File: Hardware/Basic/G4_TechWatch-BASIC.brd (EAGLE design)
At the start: 38 x 38 mm, 44 parts, among them U2 NRF52832_MODULE_MDBT42

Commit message: End Of Class Schematic
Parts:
- added C2: 1u, LinnesLab-Passives:C0603
- added R8, R9: 10k, LinnesLab-Passives:R0603
- added SW1, SW2, SW5: SWITCH.MOM, LinnesLab-Switches:TACTILE_SWITCH_SMD_6.2MM_TALL
- added U4: PCF8523, LinnesLab-Clocks:SO8
- added XTAL3: 32.7680kHz, LinnesLab-Clocks:2-SMD.NOLEAD.2.0MMTO1.2MM
- moved D5 10.8 mm to (12.0, 16.7)
- moved C20 10.8 mm to (17.6, 24.8)
- moved C21 10.8 mm to (23.6, 24.7)
- moved C5 10.8 mm to (16.9, 17.8)
- moved C6 10.8 mm to (23.0, 17.8)
- moved CHRG2 10.8 mm to (20.4, 24.8)
- moved D4 10.8 mm to (12.0, 18.8)
- moved LDO2 10.8 mm to (19.9, 17.7)
- moved R11 10.8 mm to (22.6, 27.4)
- moved R12 10.8 mm to (20.5, 21.8)
- moved R13 10.8 mm to (13.0, 27.6)
- moved R14 10.8 mm to (13.0, 24.3)
- moved C7 10.7 mm to (18.9, 35.3)
- moved C12 10.7 mm to (17.8, 31.3)
- moved L2 10.7 mm to (16.9, 35.5)
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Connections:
- new net N$16: SW1.A1, SW1.A2
- new net N$18: SW1.B1, SW1.B2
- new net N$19: U4.2, XTAL3.P$1
- new net N$20: U4.1, XTAL3.P$2
- new net N$22: SW2.A1, SW2.A2
- new net N$23: SW2.B1, SW2.B2
- new net N$24: SW5.A1, SW5.A2
- new net N$25: SW5.B1, SW5.B2
- new net VBATT: U4.3
- net 3.3V: now also C2.1, R8.2, R9.2, U4.8
- net GND: now also C2.2, U4.4
- net SCL: now also R8.1, U4.6
- net SDA: now also R9.1, U4.5

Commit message: Updated Schematics
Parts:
- moved SW5 44.6 mm to (31.0, 5.00), turned to 180 degrees
- moved SW2 30.2 mm to (19.0, 5.00), turned to 180 degrees
- moved C6 17.2 mm to (23.2, 35.0)
- moved R4 17.2 mm to (29.0, 13.8)
- moved SW1 15.8 mm to (7.00, 5.00), turned to 180 degrees
- moved R15 9.75 mm to (15.0, 13.9)
- moved C18 7.39 mm to (22.3, 30.5)
- moved C16 7.08 mm to (24.0, 30.5)
- moved R7 5.47 mm to (7.09, 14.1)
- moved R6 5.20 mm to (7.42, 16.9)
- moved R9 1.42 mm to (12.7, 33.1)
- moved XTAL3 0.89 mm to (2.51, 34.2)
- moved C2 0.53 mm to (8.51, 36.4)
- moved U4 0.47 mm to (6.71, 32.9)
- moved R8 0.25 mm to (11.2, 33.1)
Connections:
- net N$16 renamed SW1
- net N$22 renamed SW2
- net N$24 renamed SW3
- net VBATT renamed VBAT
- removed net N$18: SW1.B1, SW1.B2
- removed net N$23: SW2.B1, SW2.B2
- removed net N$25: SW5.B1, SW5.B2
- net GND: now also SW1.B1, SW1.B2, SW2.B1, SW2.B2, SW5.B1, SW5.B2, USB2.S1, USB2.S2, USB2.S3, USB2.S4, USB2.S5, USB2.S6
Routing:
- added copper zone on layer 16, net 3.3V
- added copper zone on layer 1, net GND

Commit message: Schematic Step 1 Done
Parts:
- removed SD2: (no value), LinnesLab-Connectors:MICROSD
- removed USB2: USB.MICRO-BIGGERPADS, LinnesLab-Connectors:USB-MICRO-01.BIGGERPADS
- added J1: FTDI_DEVICESMD, LinnesLab-Connectors:FTDI-SMD
- moved D1 22.2 mm to (25.2, 16.1)
- moved C14 22.0 mm to (27.9, 16.3)
- moved SW3 13.1 mm to (35.8, 34.9), turned to 270 degrees
- moved R13 11.9 mm to (1.32, 25.4)
- moved LED4 10.4 mm to (35.4, 20.2)
- moved R14 9.80 mm to (3.28, 25.2)
- moved R5 9.57 mm to (35.4, 17.1)
- moved SW4 9.05 mm to (32.2, 17.3)
- moved LED3 7.75 mm to (35.5, 22.3)
- moved CORTEX1 5.79 mm to (35.6, 29.1), turned to 270 degrees
- moved C15 5.32 mm to (2.74, 29.0)
- moved C17 5.32 mm to (5.41, 28.9)
- moved C13 5.32 mm to (1.35, 28.8)
- moved C19 5.32 mm to (4.09, 28.9)
- moved D4 3.94 mm to (11.9, 14.9)
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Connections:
- removed net CD1: SD2.CD1
- removed net CD2: SD2.CD2
- removed net SD.CS: SD2.2
- removed net USB+: USB2.3
- removed net USB-: USB2.2
- net 3.3V: no longer SD2.4
- net GND: no longer SD2.6, SD2.MT1, SD2.MT2, USB2.5, USB2.S1, USB2.S2, USB2.S3, USB2.S4, USB2.S5, USB2.S6
- net MISO: no longer SD2.7
- net MOSI: no longer SD2.3
- net SCK: no longer SD2.5
- net V_USB: no longer USB2.1

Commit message: End of Class 09/21/2022
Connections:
- removed net BATT: R13.1, R14.2
- new net AIN4/BATT: R13.1, R14.2, U2.5
- net CHRG.STAT: now also U2.4
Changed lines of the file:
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@@
 <drawing>
 <settings>
-<setting alwaysvectorfont="yes"/>
+<setting alwaysvectorfont="no"/>
 <setting verticaltext="up"/>
 </settings>
@@
 <contactref element="R12" pad="1"/>
 <contactref element="CHRG2" pad="1"/>
+<contactref element="U2" pad="4"/>
+<wire x1="17.1657" y1="25.715" x2="23.9496" y2="29.0164" width="0" layer="19" extent="1-1"/>
 <wire x1="17.6412" y1="21.844" x2="17.1657" y2="25.715" width="0" layer="19" extent="1-1"/>
-</signal>
-<signal name="BATT">
-<contactref element="R13" pad="1"/>
-<contactref element="R14" pad="2"/>
-<wire x1="1.3208" y1="24.5246" x2="3.2766" y2="26.0976" width="0" layer="19" extent="1-1"/>
 </signal>
 <signal name="VIN">
@@
 <contactref element="U4" pad="3"/>
 </signal>
+<signal name="AIN4/BATT">
+<contactref element="U2" pad="5"/>
+<contactref element="R13" pad="1"/>
+<contactref element="R14" pad="2"/>
+<wire x1="3.2766" y1="26.0976" x2="23.9496" y2="28.3164" width="0" layer="19" extent="1-1"/>
+<wire x1="1.3208" y1="24.5246" x2="3.2766" y2="26.0976" width="0" layer="19" extent="1-1"/>
+</signal>
 </signals>

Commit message: Weekly commit for class
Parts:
- moved R7 19.2 mm to (26.1, 16.5), turned to 270 degrees
- moved C18 18.6 mm to (27.1, 13.2)
- moved C6 18.0 mm to (7.14, 23.8)
- moved C17 15.5 mm to (14.1, 16.1), turned to 90 degrees
- moved C16 15.2 mm to (27.9, 16.5), turned to 90 degrees
- moved C15 14.9 mm to (10.9, 16.6)
- moved C19 14.8 mm to (12.3, 16.6), turned to 90 degrees
- moved C13 14.8 mm to (9.55, 16.6)
- moved XTAL2 11.7 mm to (25.4, 23.5), flipped to the bottom
- moved L2 10.4 mm to (19.5, 26.2), turned to 0 degrees
- moved R11 9.37 mm to (11.3, 28.9)
- moved R6 8.46 mm to (15.8, 16.3), turned to 90 degrees
- moved C7 8.20 mm to (19.5, 27.5), turned to 180 degrees
- moved C12 7.94 mm to (19.0, 24.1)
- moved C21 7.25 mm to (15.9, 29.2)
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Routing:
- net 3.3V: track 0.00 -> 19.1 mm, vias 0 -> 4
- net N$11: track 0.00 -> 5.85 mm
- net N$15: track 0.00 -> 5.50 mm
- net N$12: track 0.00 -> 5.15 mm
- net SDA: track 0.00 -> 3.88 mm
- net N$8: track 0.00 -> 3.68 mm
- net N$5: track 0.00 -> 3.68 mm
- net RESET: track 0.00 -> 2.40 mm
- net N$1: track 0.00 -> 2.17 mm
- net SWO: track 0.00 -> 2.16 mm
- net N$7: track 0.00 -> 2.09 mm
- net N$3: track 0.00 -> 2.09 mm
- net N$2: track 0.00 -> 2.04 mm
- net N$13: track 0.00 -> 1.99 mm
- net SCL: track 0.00 -> 1.83 mm
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
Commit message: Commit before leaving class
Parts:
- flipped XTAL2 to the top
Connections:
- removed net AIN4/BATT: R13.1, R14.2, U2.5
- new net AIN7/BATT: R13.1, R14.2, U2.8
- new net D7/SD.CS: U2.20
- net CS.OLED: now also U2.30
- net DC.OLED: now also U2.17
- net DTR: now also J1.DTR
- net GND: now also J1.CTS, J1.GND
- net RESET.OLED: now also U2.16
- net RXD: now also J1.TXO
- net SW1: now also U2.25
- net SW2: now also U2.29
- net SW3: now also U2.5
- net TXD: now also J1.RXI
- net V_USB: now also J1.VCC
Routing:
- net 3.3V: track 19.1 -> 0.00 mm, vias 4 -> 0
- net N$11: track 5.85 -> 0.00 mm
- net N$15: track 5.50 -> 0.00 mm
- net N$12: track 5.15 -> 0.00 mm
- net SDA: track 3.88 -> 0.00 mm
- net N$8: track 3.68 -> 0.00 mm
- net N$5: track 3.68 -> 0.00 mm
- net RESET: track 2.40 -> 0.00 mm
- net N$1: track 2.17 -> 0.00 mm
- net SWO: track 2.16 -> 0.00 mm
- net N$7: track 2.09 -> 0.00 mm
- net N$3: track 2.09 -> 0.00 mm
- net N$2: track 2.04 -> 0.00 mm
- net N$13: track 1.99 -> 0.00 mm
- net SCL: track 1.83 -> 0.00 mm
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
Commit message: Board Completed
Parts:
- removed C19: 2.2uF, LinnesLab-Passives:C0402
- removed C20, C21: 4.7u, LinnesLab-Passives:C0603
- removed CHRG2: MCP73831, LinnesLab-Power:SOT23-5
- removed CORTEX1: CORTEX_DEBUG_PTH, LinnesLab-Connectors:2X5-PTH-1.27MM
- removed D4, D5: (no value), LinnesLab-DiscreteSemi:USC
- removed L2: 10u, LinnesLab-Passives:L0603
- removed LDO2: MIC5504, LinnesLab-Power:SOT23-5
- removed LED3: RED, LinnesLab-LED:LED-0603
- removed LED4: BLUE, LinnesLab-LED:LED-0603
- removed R13, R14, R15: 100k, LinnesLab-Passives:R0603
- removed U4: PCF8523, LinnesLab-Clocks:SO8
- removed XTAL3: 32.7680kHz, LinnesLab-Clocks:2-SMD.NOLEAD.2.0MMTO1.2MM
- added C1: 1u, LinnesLab-Passives:C0603
- added C3, C4: (no value), LinnesLab-Passives:C0603
- added CHRG1: MCP73831, LinnesLab-Power:SOT23-5
- added D2, D3: (no value), LinnesLab-DiscreteSemi:USC
- added DEBUG1: CORTEX_DEBUG_PTH, LinnesLab-Connectors:2X5-PTH-1.27MM
- added L1: 10u, LinnesLab-Passives:L0603
- added LDO1: MIC5504, LinnesLab-Power:SOT23-5
- added LED1: RED, LinnesLab-LED:LED-0603
- added LED2: BLUE, LinnesLab-LED:LED-0603
- added R1, R10, R2: 10k, LinnesLab-Passives:R0603
- added U1: NRF52832_MODULE_MDBT42, LinnesLab-Microcontrollers:BLE_MODULE_RAYTAC_MDBT42
- added XTAL1: 32.768kHz, LinnesLab-Clocks:2-SMD.NOLEAD.2.0MMTO1.2MM
- C10: value 300p -> 4.7u
- C11: value 300p -> 100n
- C12: value 10u -> 10uF; device LinnesLab-Passives:C0805 -> LinnesLab-Passives:C0603
- C14: value 100n -> 2.2uF; device LinnesLab-Passives:C0603 -> LinnesLab-Passives:C0402
- C16: value 10uF -> 2.2uF; device LinnesLab-Passives:C0603 -> LinnesLab-Passives:C0402
- C18: value 2.2uF -> 1u; device LinnesLab-Passives:C0402 -> LinnesLab-Passives:C0603
- C2: value 1u -> 10u; device LinnesLab-Passives:C0603 -> LinnesLab-Passives:C0805
- C5, C6: value 1u -> 300p
- C7: value 1u -> 4.7u
- C8, C9: value (none) -> 1u
- R11: value (none) -> 10k
- R12: value 100k -> 390k
- R3: value 1k -> 100k
- R5: value 10k -> 1k
- R6: value 10k -> (none)
- R7: value 390k -> 100k
- R8, R9: value 10k -> 100k
- SW1, SW2: value SWITCH.MOM -> (none); device LinnesLab-Switches:TACTILE_SWITCH_SMD_6.2MM_TALL -> LinnesLab-Switches:BUTTON-GULLWING
- SW3, SW4: value (none) -> SWITCH.MOM; device LinnesLab-Switches:BUTTON-GULLWING -> LinnesLab-Switches:TACTILE_SWITCH_SMD_6.2MM_TALL
- U2: value NRF52832_MODULE_MDBT42 -> PCF8523; device LinnesLab-Microcontrollers:BLE_MODULE_RAYTAC_MDBT42 -> LinnesLab-Clocks:SO8
- XTAL2: value 32.768kHz -> 32.7680kHz
- moved SW1 41.6 mm to (35.0, 35.7), turned to 0 degrees
- moved SW3 37.7 mm to (12.7, 5.03), turned to 180 degrees
- moved R3 31.2 mm to (6.02, 14.5), turned to 270 degrees
- moved C10 30.7 mm to (4.62, 16.9), turned to 90 degrees
- moved C18 27.3 mm to (8.20, 32.9), turned to 180 degrees
- moved C9 26.5 mm to (3.89, 2.84), turned to 270 degrees
- moved R7 24.9 mm to (5.31, 2.84), turned to 90 degrees
- moved C6 24.9 mm to (31.7, 19.9), turned to 0 degrees
- moved XTAL2 24.3 mm to (2.21, 30.7), turned to 90 degrees
- moved R9 23.6 mm to (3.20, 11.2)
- moved U2 22.1 mm to (6.40, 29.4)
- moved C7 21.1 mm to (7.09, 10.4), turned to 90 degrees
- moved C8 20.9 mm to (4.67, 12.8), turned to 90 degrees
- moved R8 20.3 mm to (3.20, 14.2)
- moved SW2 19.7 mm to (34.9, 16.6), turned to 90 degrees
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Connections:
- net 3.3V: now also C16.2, C18.1, C2.2, C9.1, D3.-, DEBUG1.1, LDO1.5, R1.2, R10.2, R2.2, R7.2, U1.11, U2.8; no longer C12.2, C19.2, C2.1, C6.1, CORTEX1.1, D1.-, LDO2.5, R15.2, R5.2, R8.2, R9.2, U2.11, U4.8
- net AIN7/BATT: now also R8.1, R9.2, U1.8; no longer R13.1, R14.2, U2.8
- net CHRG.STAT: now also CHRG1.1, R3.1, U1.4; no longer CHRG2.1, R12.1, U2.4
- net CS.OLED: now also U1.30; no longer U2.30
- net D7/SD.CS: now also U1.20; no longer U2.20
- net DC.OLED: now also U1.17; no longer U2.17
- net DFU: now also SW1.3, U1.34; no longer SW3.3, U2.34
- net DTR: now also C11.1; no longer C14.1
- net FRST: now also U1.38; no longer U2.38
- net GND: now also C1.2, C14.1, C18.2, C2.1, C3.1, C4.2, C5.2, C7.1, CHRG1.2, DEBUG1.3, DEBUG1.5, DEBUG1.7, DEBUG1.9, LDO1.2, LED1.C, LED2.C, R12.2, R7.1, R9.1, SW1.1, SW2.3, SW3.B1, SW3.B2, SW4.B1, SW4.B2, U1.1, U1.12, U1.24, U1.39, U2.4; no longer C11.2, C18.1, C19.1, C2.2, C20.2, C21.1, C5.1, C7.2, CHRG2.2, CORTEX1.3, CORTEX1.5, CORTEX1.7, CORTEX1.9, LDO2.2, LED3.C, LED4.C, R14.1, R15.1, R7.2, SW1.B1, SW1.B2, SW2.B1, SW2.B2, SW3.1, SW4.3, U2.1, U2.12, U2.24, U2.39, U4.4
- net LED1: now also R4.2, U1.31; no longer R3.2, U2.31
- net LED2: now also R5.2, U1.33; no longer R4.2, U2.33
- net MISO: now also U1.28; no longer U2.28
- net MOSI: now also U1.27; no longer U2.27
- net N$1: now also R11.2; no longer R6.2
- net N$10: now also LED2.A, R5.1; no longer LED4.A, R4.1
- net N$11: now also L1.1, U1.10; no longer L2.1, U2.10
- net N$12: now also C1.1, L1.2, U1.9; no longer C7.1, L2.2, U2.9
- net N$13: now also C12.2; no longer C16.2
- net N$14: now also DEBUG1.8; no longer CORTEX1.8
- net N$15: now also C14.2; no longer C18.2
- net N$17: now also CHRG1.5, R6.2; no longer CHRG2.5, R11.2
- net N$19: now also U2.2, XTAL2.P$1; no longer U4.2, XTAL3.P$1
- net N$2: now also R12.1; no longer R7.1
- net N$20: now also U2.1, XTAL2.P$2; no longer U4.1, XTAL3.P$2
- net N$3: now also C15.2; no longer C13.2
- net N$4: now also C3.2, U1.13, XTAL1.P$1; no longer C8.2, U2.13, XTAL2.P$1
- net N$5: now also C15.1; no longer C13.1
- net N$6: now also C4.1, U1.14, XTAL1.P$2; no longer C9.1, U2.14, XTAL2.P$2
- net N$7: now also C13.2; no longer C15.2
- net N$8: now also C13.1; no longer C15.1
- net N$9: now also LED1.A, R4.1; no longer LED3.A, R3.1
- net P0.09/NFC1: now also C5.1, U1.22; no longer C11.1, U2.22
- net P0.10/NFC2: now also C6.1, U1.23; no longer C10.1, U2.23
- net RESET: now also C11.2, D3.+, DEBUG1.10, R10.1, SW2.1, U1.35; no longer C14.2, CORTEX1.10, D1.+, R5.1, SW4.1, U2.35
- net RESET.OLED: now also U1.16; no longer U2.16
- net RXD: now also U1.21; no longer U2.21
- net SCK: now also U1.26; no longer U2.26
- net SCL: now also R2.1, U1.3, U2.6; no longer R8.1, U2.3, U4.6
- net SDA: now also R1.1, U1.2, U2.5; no longer R9.1, U2.2, U4.5
- net SW1: now also SW3.A1, SW3.A2, U1.25; no longer SW1.A1, SW1.A2, U2.25
- net SW2: now also SW4.A1, SW4.A2, U1.29; no longer SW2.A1, SW2.A2, U2.29
- net SW3: now also U1.5; no longer U2.5
- net SWCLK: now also DEBUG1.4, U1.36; no longer CORTEX1.4, U2.36
- net SWDIO: now also DEBUG1.2, U1.37; no longer CORTEX1.2, U2.37
- net SWO: now also DEBUG1.6, U1.32; no longer CORTEX1.6, U2.32
- net TXD: now also U1.19; no longer U2.19
- net VBAT: now also U2.3; no longer U4.3
- net VIN: now also C7.2, C8.2, CHRG1.4, D1.-, D2.-, LDO1.1, LDO1.3, R3.2; no longer C21.2, C5.2, CHRG2.4, D4.-, D5.-, LDO2.1, LDO2.3, R12.2
- net VLIPO: now also C10.1, CHRG1.3, D1.+, R8.2; no longer C20.1, CHRG2.3, D4.+, R13.2
- net V_USB: now also D2.+; no longer D5.+
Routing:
- net GND: track 0.00 -> 100.7 mm, vias 0 -> 15
- net SW3: track 0.00 -> 52.0 mm, vias 0 -> 2
- net SW1: track 0.00 -> 31.5 mm, vias 0 -> 2
- net SW2: track 0.00 -> 30.2 mm, vias 0 -> 2
- net AIN7/BATT: track 0.00 -> 29.4 mm, vias 0 -> 2
- net RESET: track 0.00 -> 25.3 mm, vias 0 -> 2
- net RXD: track 0.00 -> 24.7 mm, vias 0 -> 1
- net CHRG.STAT: track 0.00 -> 23.6 mm, vias 0 -> 2
- net TXD: track 0.00 -> 23.5 mm, vias 0 -> 1
- net CS.OLED: track 0.00 -> 20.7 mm, vias 0 -> 2
- net DTR: track 0.00 -> 19.1 mm, vias 0 -> 1
- net VIN: track 0.00 -> 18.4 mm
- net SCK: track 0.00 -> 17.3 mm, vias 0 -> 2
- net MOSI: track 0.00 -> 17.1 mm, vias 0 -> 2
- net RESET.OLED: track 0.00 -> 16.2 mm, vias 0 -> 2
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- added copper zone on layer 1, net 3.3V
- added copper zone on layer 16, net GND
- removed copper zone on layer 16, net 3.3V
- removed copper zone on layer 1, net GND

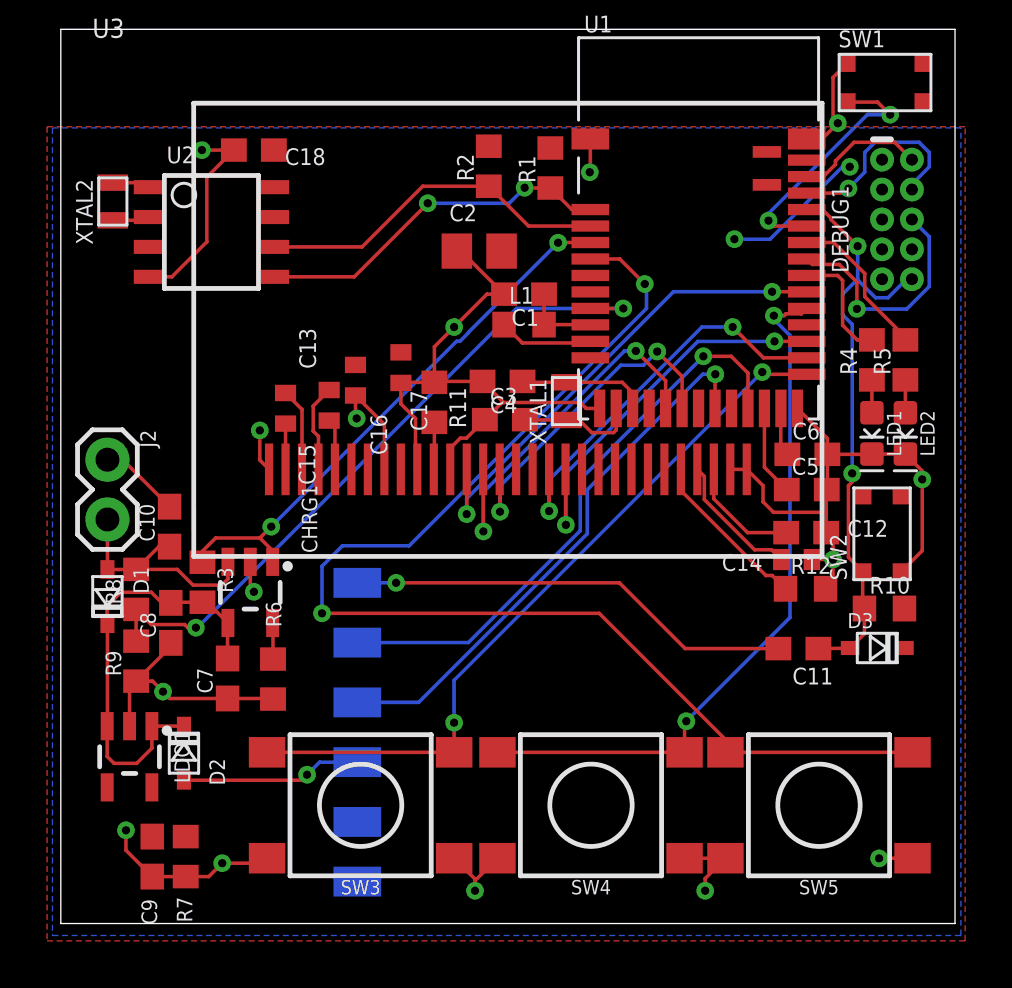
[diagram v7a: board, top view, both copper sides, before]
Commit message: Added Ground Vias
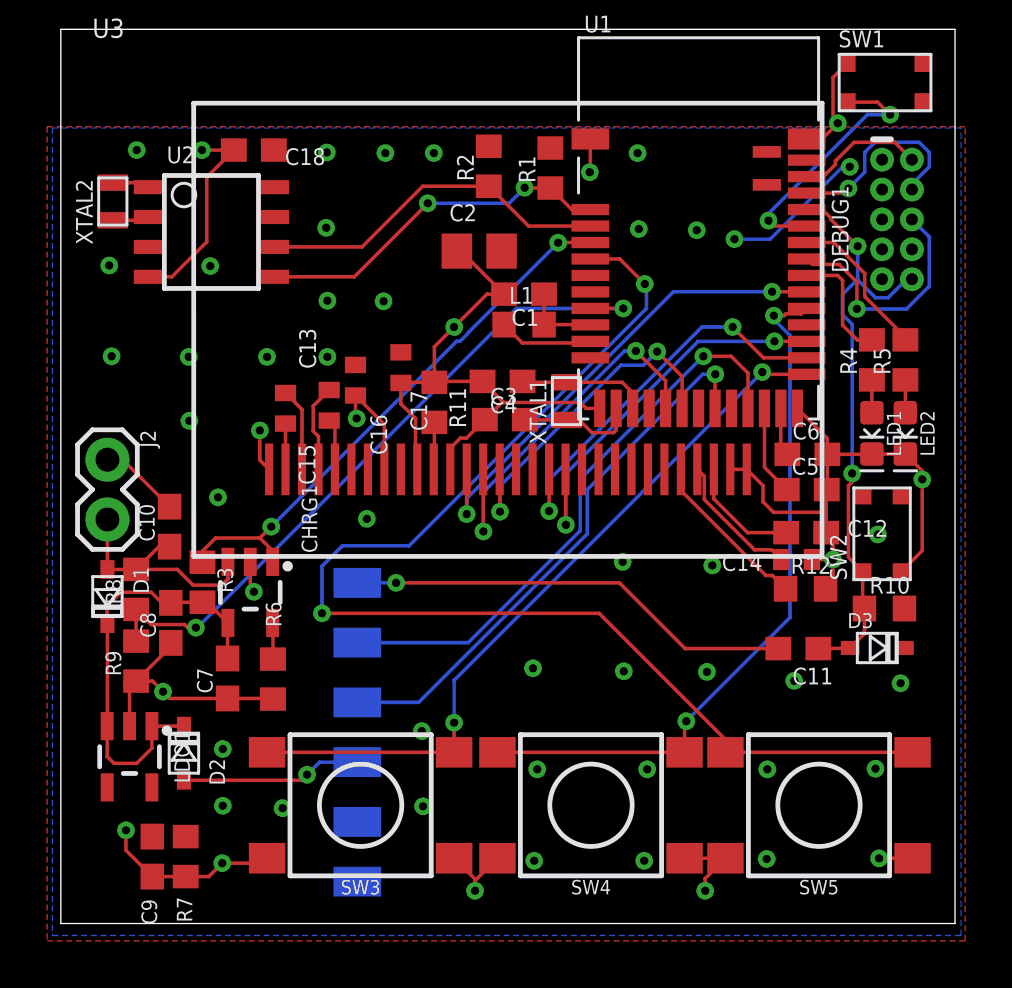
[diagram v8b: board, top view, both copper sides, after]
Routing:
- net GND: vias 15 -> 54
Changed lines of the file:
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@@
 <wire x1="4.6346" y1="9.564" x2="4.3434" y2="9.8552" width="0.1524" layer="1"/>
 <wire x1="33.4266" y1="36.5628" x2="32.8168" y2="35.953" width="0.1524" layer="1"/>
+<via x="11.303" y="32.766" extent="1-16" drill="0.35"/>
+<via x="13.7922" y="32.7406" extent="1-16" drill="0.35"/>
+<via x="15.8496" y="32.7406" extent="1-16" drill="0.35"/>
+<via x="11.2776" y="29.5656" extent="1-16" drill="0.35"/>
+<via x="24.5618" y="29.5148" extent="1-16" drill="0.35"/>
+<via x="27.0256" y="29.464" extent="1-16" drill="0.35"/>
+<via x="24.511" y="32.7406" extent="1-16" drill="0.35"/>
+<via x="3.2258" y="32.8676" extent="1-16" drill="0.35"/>
+<via x="2.0574" y="27.9654" extent="1-16" drill="0.35"/>
+<via x="6.35" y="27.94" extent="1-16" drill="0.35"/>
+<via x="11.3284" y="26.4668" extent="1-16" drill="0.35"/>
+<via x="13.716" y="26.4414" extent="1-16" drill="0.35"/>
+<via x="11.3284" y="24.0792" extent="1-16" drill="0.35"/>
+<via x="8.763" y="24.0792" extent="1-16" drill="0.35"/>
+<via x="5.4356" y="24.0792" extent="1-16" drill="0.35"/>
+<via x="2.159" y="24.1046" extent="1-16" drill="0.35"/>
+<via x="5.461" y="21.3614" extent="1-16" drill="0.35"/>
+<via x="6.6802" y="18.1102" extent="1-16" drill="0.35"/>
+<via x="13.0048" y="17.1958" extent="1-16" drill="0.35"/>
+<via x="6.8834" y="7.4168" extent="1-16" drill="0.35"/>
+<via x="6.8834" y="5.0038" extent="1-16" drill="0.35"/>
+<via x="9.4234" y="4.9022" extent="1-16" drill="0.35"/>
+<via x="15.3924" y="4.9784" extent="1-16" drill="0.35"/>
+<via x="15.3416" y="8.1788" extent="1-16" drill="0.35"/>
+<via x="20.1168" y="2.667" extent="1-16" drill="0.35"/>
+<via x="24.7904" y="2.667" extent="1-16" drill="0.35"/>
+<via x="24.9174" y="6.5532" extent="1-16" drill="0.35"/>
+<via x="20.2438" y="6.5532" extent="1-16" drill="0.35"/>
+<via x="20.066" y="10.8458" extent="1-16" drill="0.35"/>
+<via x="23.9268" y="10.7188" extent="1-16" drill="0.35"/>
+<via x="23.876" y="15.367" extent="1-16" drill="0.35"/>
+<via x="27.686" y="15.2146" extent="1-16" drill="0.35"/>
+<via x="27.4574" y="10.6934" extent="1-16" drill="0.35"/>
+<via x="31.1658" y="10.3124" extent="1-16" drill="0.35"/>
+<via x="35.687" y="10.2108" extent="1-16" drill="0.35"/>
+<via x="29.9974" y="2.7432" extent="1-16" drill="0.35"/>
+<via x="30.0228" y="6.5532" extent="1-16" drill="0.35"/>
+<via x="34.6202" y="6.5786" extent="1-16" drill="0.35"/>
+<via x="34.7218" y="16.5354" extent="1-16" drill="0.35"/>
 </signal>
 <signal name="N$4">
